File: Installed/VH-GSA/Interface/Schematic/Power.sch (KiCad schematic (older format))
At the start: 7 parts, among them P16 Anderson 15A, P17 CONN_01X03, P18 CONN_01X03, P19 CONN_01X02

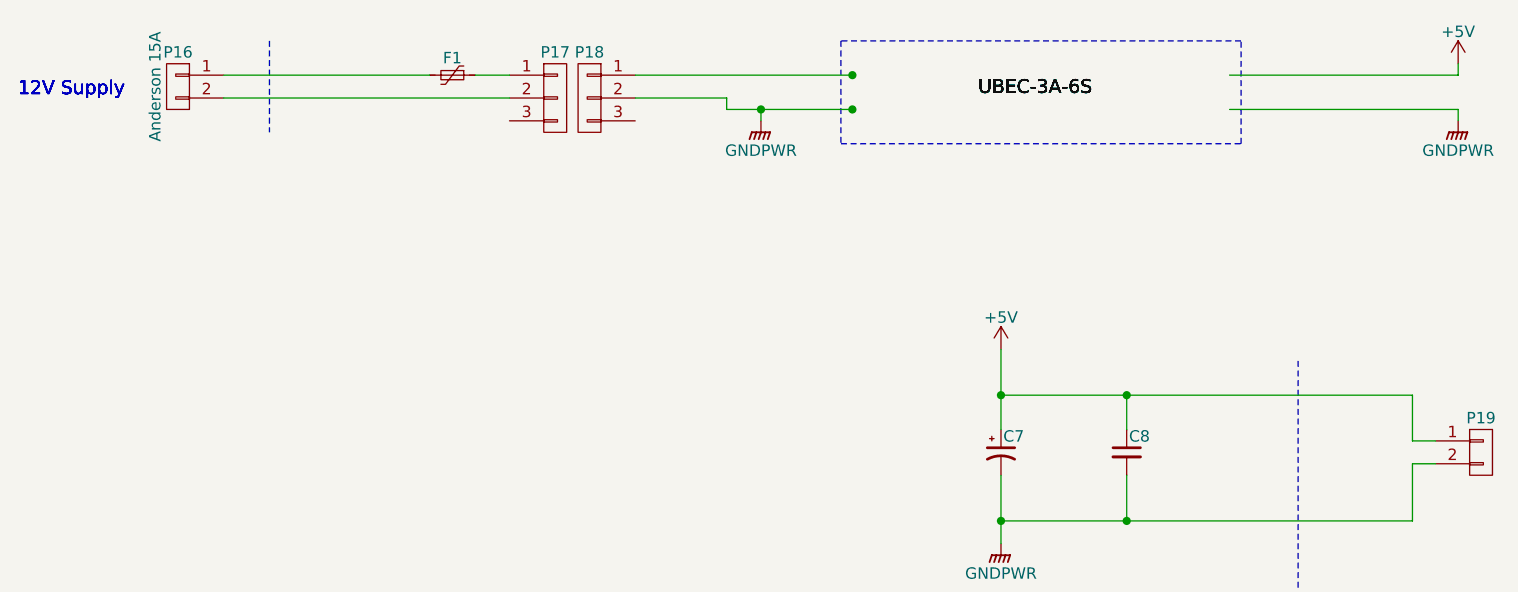
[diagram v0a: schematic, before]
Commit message: VH-GSA: Added multiple 5V sources
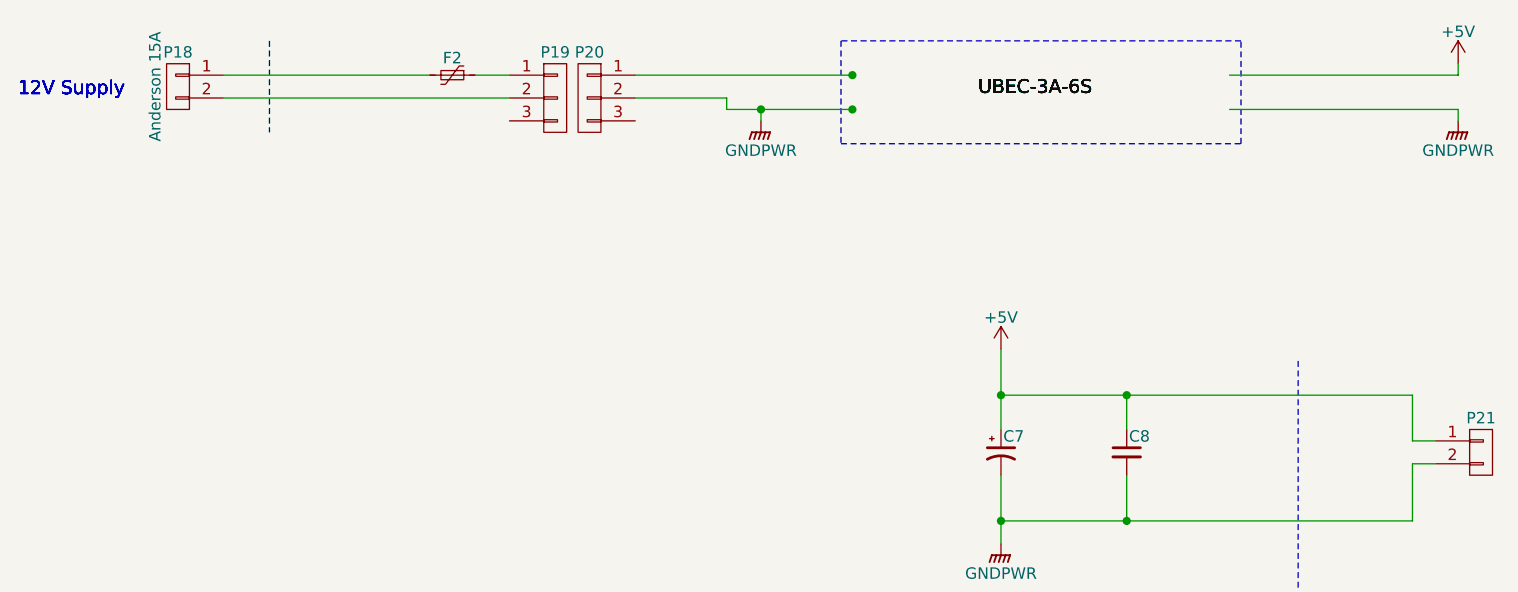
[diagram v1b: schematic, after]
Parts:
- renumbered F1 to F2, P16 to P18, P17 to P19, P18 to P20, P19 to P21
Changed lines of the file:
@@
 LIBS:valves
 LIBS:switches
+LIBS:VH-GSA-cache
 EELAYER 25 0
 EELAYER END
@@
 UBEC-3A-6S
 $Comp
-L CONN_01X03 P18
+L CONN_01X03 P20
 U 1 1 5D9DB585
 P 3050 2500
-F 0 "P18" H 3050 2700 50  0000 C CNN
+F 0 "P20" H 3050 2700 50  0000 C CNN
 F 1 "CONN_01X03" V 3150 2500 50  0001 C CNN
 F 2 "" H 3050 2500 50  0000 C CNN
@@
 $EndComp
 $Comp
-L CONN_01X03 P17
+L CONN_01X03 P19
 U 1 1 5D9DB5EA
 P 2900 2500
-F 0 "P17" H 2900 2700 50  0000 C CNN
+F 0 "P19" H 2900 2700 50  0000 C CNN
 F 1 "CONN_01X03" V 3000 2500 50  0001 C CNN
 F 2 "" H 2900 2500 50  0000 C CNN
@@
 $EndComp
 $Comp
-L Polyfuse_Small F1
+L Polyfuse_Small F2
 U 1 1 5D9DC029
 P 2450 2400
-F 0 "F1" V 2375 2400 50  0000 C CNN
+F 0 "F2" V 2375 2400 50  0000 C CNN
 F 1 "Polyfuse_Small" V 2525 2400 50  0001 C CNN
 F 2 "" H 2500 2200 50  0001 L CNN
@@
 $EndComp
 $Comp
-L CONN_01X02 P16
+L CONN_01X02 P18
 U 1 1 5D9DC29B
 P 1250 2450
-F 0 "P16" H 1250 2600 50  0000 C CNN
+F 0 "P18" H 1250 2600 50  0000 C CNN
 F 1 "Anderson 15A" V 1350 2450 50  0000 C CNN
 F 2 "" H 1250 2450 50  0000 C CNN
@@
 $EndComp
 $Comp
-L GNDPWR #PWR12
+L GNDPWR #PWR18
 U 1 1 5D9DD65D
 P 3800 2600
-F 0 "#PWR12" H 3800 2400 50  0001 C CNN
+F 0 "#PWR18" H 3800 2400 50  0001 C CNN
 F 1 "GNDPWR" H 3800 2470 50  0000 C CNN
 F 2 "" H 3800 2550 50  0000 C CNN
@@
 $EndComp
 $Comp
-L +5V #PWR15
+L +5V #PWR21
 U 1 1 5D9DF51D
 P 6850 2350
-F 0 "#PWR15" H 6850 2200 50  0001 C CNN
+F 0 "#PWR21" H 6850 2200 50  0001 C CNN
 F 1 "+5V" H 6850 2490 50  0000 C CNN
 F 2 "" H 6850 2350 50  0000 C CNN
@@
 $EndComp
 $Comp
-L GNDPWR #PWR16
+L GNDPWR #PWR22
 U 1 1 5D9DF5C3
 P 6850 2600
-F 0 "#PWR16" H 6850 2400 50  0001 C CNN
+F 0 "#PWR22" H 6850 2400 50  0001 C CNN
 F 1 "GNDPWR" H 6850 2470 50  0000 C CNN
 F 2 "" H 6850 2550 50  0000 C CNN
@@
 	3800 2550 3800 2600
 $Comp
-L +5V #PWR13
+L +5V #PWR19
 U 1 1 5DA74517
 P 4850 3600
-F 0 "#PWR13" H 4850 3450 50  0001 C CNN
+F 0 "#PWR19" H 4850 3450 50  0001 C CNN
 F 1 "+5V" H 4850 3740 50  0000 C CNN
 F 2 "" H 4850 3600 50  0000 C CNN
@@
 $EndComp
 $Comp
-L GNDPWR #PWR14
+L GNDPWR #PWR20
 U 1 1 5DA7459A
 P 4850 4450
-F 0 "#PWR14" H 4850 4250 50  0001 C CNN
+F 0 "#PWR20" H 4850 4250 50  0001 C CNN
 F 1 "GNDPWR" H 4850 4320 50  0000 C CNN
 F 2 "" H 4850 4400 50  0000 C CNN
@@
 $EndComp
 $Comp
-L CONN_01X02 P19
+L CONN_01X02 P21
 U 1 1 5DA746DD
 P 6950 4050
-F 0 "P19" H 6950 4200 50  0000 C CNN
+F 0 "P21" H 6950 4200 50  0000 C CNN
 F 1 "CONN_01X02" V 7050 4050 50  0001 C CNN
 F 2 "" H 6950 4050 50  0000 C CNN

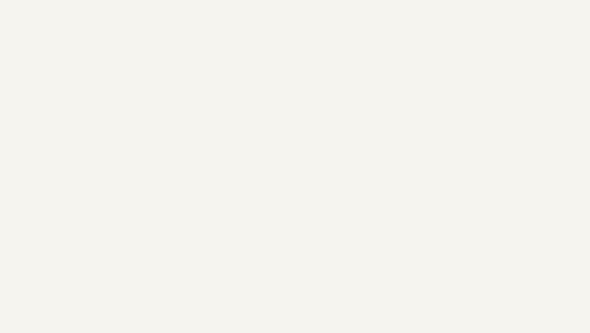
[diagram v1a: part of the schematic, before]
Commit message: VH-GSA: Removed Flarm loop through
This version assumes that the Flatm Redbox is connected to the S8
Vario.
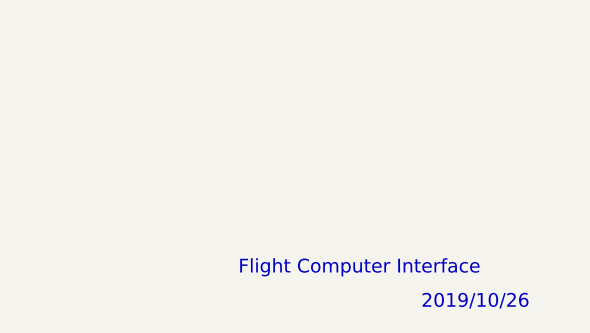
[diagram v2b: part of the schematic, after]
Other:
- note added: "2019/10/26"
- note added: "Flight Computer Interface"
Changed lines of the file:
@@
 $EndComp
 $Comp
-L GNDPWR #PWR18
+L GNDPWR #PWR20
 U 1 1 5D9DD65D
 P 3800 2600
-F 0 "#PWR18" H 3800 2400 50  0001 C CNN
+F 0 "#PWR20" H 3800 2400 50  0001 C CNN
 F 1 "GNDPWR" H 3800 2470 50  0000 C CNN
 F 2 "" H 3800 2550 50  0000 C CNN
@@
 $EndComp
 $Comp
-L +5V #PWR21
+L +5V #PWR23
 U 1 1 5D9DF51D
 P 6850 2350
-F 0 "#PWR21" H 6850 2200 50  0001 C CNN
+F 0 "#PWR23" H 6850 2200 50  0001 C CNN
 F 1 "+5V" H 6850 2490 50  0000 C CNN
 F 2 "" H 6850 2350 50  0000 C CNN
@@
 $EndComp
 $Comp
-L GNDPWR #PWR22
+L GNDPWR #PWR24
 U 1 1 5D9DF5C3
 P 6850 2600
-F 0 "#PWR22" H 6850 2400 50  0001 C CNN
+F 0 "#PWR24" H 6850 2400 50  0001 C CNN
 F 1 "GNDPWR" H 6850 2470 50  0000 C CNN
 F 2 "" H 6850 2550 50  0000 C CNN
@@
 	3800 2550 3800 2600
 $Comp
-L +5V #PWR19
+L +5V #PWR21
 U 1 1 5DA74517
 P 4850 3600
-F 0 "#PWR19" H 4850 3450 50  0001 C CNN
+F 0 "#PWR21" H 4850 3450 50  0001 C CNN
 F 1 "+5V" H 4850 3740 50  0000 C CNN
 F 2 "" H 4850 3600 50  0000 C CNN
@@
 $EndComp
 $Comp
-L GNDPWR #PWR20
+L GNDPWR #PWR22
 U 1 1 5DA7459A
 P 4850 4450
-F 0 "#PWR20" H 4850 4250 50  0001 C CNN
+F 0 "#PWR22" H 4850 4250 50  0001 C CNN
 F 1 "GNDPWR" H 4850 4320 50  0000 C CNN
 F 2 "" H 4850 4400 50  0000 C CNN
@@
 Wire Notes Line
 	6150 3650 6150 4650
+Text Notes 7350 7500 0    60   ~ 0
+Flight Computer Interface
+Text Notes 8150 7650 0    60   ~ 0
+2019/10/26
 $EndSCHEMATC
